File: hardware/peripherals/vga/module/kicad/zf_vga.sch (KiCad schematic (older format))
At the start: 51 parts, among them J2 Z-FIGHTER Expansion Port, J3 DB15_Female, J4 DB9_Male, J5 DB9_Male, SW1 SW_DIP_x03, U1 4040, U10 74HC165, U11 AS6C6264, U12 74HC541, U13 74HC541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

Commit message: VGA Rev. 2
Fixed VGA connector footprint, expanded joystick connectors for '241 buffer, added jumper-selectable interrupt generator
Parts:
- added JP1: Jumper, symbol Device:Jumper
- added Q1: BC547, Package_TO_SOT_THT:TO-92_HandSolder, symbol Transistor_BJT:BC547
- added R10: 1K, Resistor_THT:R_Axial_DIN0207_L6.3mm_D2.5mm_P7.62mm_Horizontal, symbol Device:R
- R1, R2: value R -> 220
- R3: value R -> 200
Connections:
- net DATARDY: now also J2.20 (Pin_20); no longer J2.18 (Pin_18)
- net GND: now also J4.6, J5.6, Q1.3 (E); no longer J4.8, J5.8
- net PA0: now also J4.2, J5.2; no longer J4.1, J5.1
- net PA1: now also J4.3, J5.3; no longer J4.2, J5.2
- net PA2: now also J4.4, J5.4; no longer J4.3, J5.3
- net PA3: now also J4.5, J5.5; no longer J4.4, J5.4
- net PA4: no longer J4.5, J5.5
- net PA5: no longer J4.6, J5.6
- net PC5: now also J4.8; no longer J4.9
- net PC6: now also J5.7; no longer J5.9
- net VCC: now also J4.1, J5.1; no longer J4.7, J5.7
- net PC7: now reaches J2.12 (Pin_12)
- net PC7: now also J5.8
- net #INT: now reaches J2.29 (Pin_29)
- net #INT: now also JP1.2
- net VSYNC: now reaches U4.12 (IO8)
- net VSYNC: now also R10.1
- new net: JP1.1, Q1.1 (C)
- new net: Q1.2 (B), R10.2
- new net PC4: J2.18 (Pin_18), J4.7
- no-connect marks 32 -> 30
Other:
- note added: "Interrupt generator"
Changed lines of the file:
@@
 Text GLabel 7550 3450 2    50   Input ~ 0
 D0
-Text GLabel 7000 5550 0    50   Input ~ 0
-PA0
-Text GLabel 7000 5650 0    50   Input ~ 0
-PA5
 $Comp
 L power:VCC #PWR0116
 U 1 1 622CFD96
-P 6650 5850
-F 0 "#PWR0116" H 6650 5700 50  0001 C CNN
-F 1 "VCC" H 6665 6023 50  0000 C CNN
-F 2 "" H 6650 5850 50  0001 C CNN
-F 3 "" H 6650 5850 50  0001 C CNN
-	1    6650 5850
-	1    0    0    -1
-$EndComp
-Wire Wire Line
-	7000 5850 6650 5850
+P 6650 5550
+F 0 "#PWR0116" H 6650 5400 50  0001 C CNN
+F 1 "VCC" H 6665 5723 50  0000 C CNN
+F 2 "" H 6650 5550 50  0001 C CNN
+F 3 "" H 6650 5550 50  0001 C CNN
+	1    6650 5550
+	1    0    0    -1
+$EndComp
+Wire Wire Line
+	7000 5550 6650 5550
 $Comp
 L power:GND #PWR0135
 U 1 1 622D919E
-P 6650 6050
-F 0 "#PWR0135" H 6650 5800 50  0001 C CNN
-F 1 "GND" H 6655 5877 50  0000 C CNN
-F 2 "" H 6650 6050 50  0001 C CNN
-F 3 "" H 6650 6050 50  0001 C CNN
-	1    6650 6050
-	1    0    0    -1
-$EndComp
-Text GLabel 7000 5750 0    50   Input ~ 0
-PA1
-Text GLabel 7000 5950 0    50   Input ~ 0
-PA2
-Text GLabel 7000 6150 0    50   Input ~ 0
-PA3
-Text GLabel 7000 6350 0    50   Input ~ 0
-PA4
-Text GLabel 7000 6250 0    50   Input ~ 0
-PC5
+P 6650 5650
+F 0 "#PWR0135" H 6650 5400 50  0001 C CNN
+F 1 "GND" H 6655 5477 50  0000 C CNN
+F 2 "" H 6650 5650 50  0001 C CNN
+F 3 "" H 6650 5650 50  0001 C CNN
+	1    6650 5650
+	1    0    0    -1
+$EndComp
 $Comp
 L Connector:DB9_Female J4
@@
 P 5750 4100
 F 0 "R1" H 5820 4146 50  0000 L CNN
-F 1 "R" H 5820 4055 50  0000 L CNN
+F 1 "220" H 5820 4055 50  0000 L CNN
 F 2 "Resistor_THT:R_Axial_DIN0207_L6.3mm_D2.5mm_P7.62mm_Horizontal" V 5680 4100 50  0001 C CNN
 F 3 "~" H 5750 4100 50  0001 C CNN
@@
 P 5750 4450
 F 0 "R2" H 5820 4496 50  0000 L CNN
-F 1 "R" H 5820 4405 50  0000 L CNN
+F 1 "220" H 5820 4405 50  0000 L CNN
 F 2 "Resistor_THT:R_Axial_DIN0207_L6.3mm_D2.5mm_P7.62mm_Horizontal" V 5680 4450 50  0001 C CNN
 F 3 "~" H 5750 4450 50  0001 C CNN
@@
 P 5750 4800
 F 0 "R3" H 5820 4846 50  0000 L CNN
-F 1 "R" H 5820 4755 50  0000 L CNN
+F 1 "200" H 5820 4755 50  0000 L CNN
 F 2 "Resistor_THT:R_Axial_DIN0207_L6.3mm_D2.5mm_P7.62mm_Horizontal" V 5680 4800 50  0001 C CNN
 F 3 "~" H 5750 4800 50  0001 C CNN
@@
 	1    0    0    -1
 $EndComp
-Text Notes 8200 6500 0    50   ~ 0
+Text Notes 8200 6550 0    50   ~ 0
 Controller Port 2
-Text Notes 6450 6500 0    50   ~ 0
+Text Notes 6450 6550 0    50   ~ 0
 Controller Port 1
 Text Notes 8850 4950 0    50   ~ 0
@@
 Text Notes 10500 4950 0    50   ~ 0
 Upper Write Address Buffer
-Text GLabel 8750 6250 0    50   Input ~ 0
-PC6
-Text GLabel 8750 6350 0    50   Input ~ 0
-PA4
-Text GLabel 8750 6150 0    50   Input ~ 0
-PA3
-Text GLabel 8750 5950 0    50   Input ~ 0
-PA2
-Text GLabel 8750 5750 0    50   Input ~ 0
-PA1
-Text GLabel 8750 5650 0    50   Input ~ 0
-PA5
-Text GLabel 8750 5550 0    50   Input ~ 0
-PA0
 $Comp
 L power:GND #PWR0139
 U 1 1 622E4CA3
-P 8400 6050
-F 0 "#PWR0139" H 8400 5800 50  0001 C CNN
-F 1 "GND" H 8405 5877 50  0000 C CNN
-F 2 "" H 8400 6050 50  0001 C CNN
-F 3 "" H 8400 6050 50  0001 C CNN
-	1    8400 6050
-	1    0    0    -1
-$EndComp
-Wire Wire Line
-	8750 6050 8400 6050
-Wire Wire Line
-	8750 5850 8400 5850
+P 8400 5650
+F 0 "#PWR0139" H 8400 5400 50  0001 C CNN
+F 1 "GND" H 8405 5477 50  0000 C CNN
+F 2 "" H 8400 5650 50  0001 C CNN
+F 3 "" H 8400 5650 50  0001 C CNN
+	1    8400 5650
+	1    0    0    -1
+$EndComp
+Wire Wire Line
+	8750 5650 8400 5650
+Wire Wire Line
+	8750 5550 8400 5550
 $Comp
 L power:VCC #PWR0136
 U 1 1 622E4C9B
-P 8400 5850
-F 0 "#PWR0136" H 8400 5700 50  0001 C CNN
-F 1 "VCC" H 8415 6023 50  0000 C CNN
-F 2 "" H 8400 5850 50  0001 C CNN
-F 3 "" H 8400 5850 50  0001 C CNN
-	1    8400 5850
-	1    0    0    -1
-$EndComp
-Text GLabel 10200 2100 0    50   Input ~ 0
-PC6
+P 8400 5550
+F 0 "#PWR0136" H 8400 5400 50  0001 C CNN
+F 1 "VCC" H 8415 5723 50  0000 C CNN
+F 2 "" H 8400 5550 50  0001 C CNN
+F 3 "" H 8400 5550 50  0001 C CNN
+	1    8400 5550
+	1    0    0    -1
+$EndComp
 Text GLabel 10200 2000 0    50   Input ~ 0
 PC5
+Text GLabel 10200 1900 0    50   Input ~ 0
+PC4
 Text GLabel 10200 1500 0    50   Input ~ 0
 PC0
@@
 	1    0    0    -1
 $EndComp
-Text GLabel 10200 1900 0    50   Input ~ 0
+Text GLabel 10200 1800 0    50   Input ~ 0
 DATARDY
 Text GLabel 10950 3950 2    50   Input ~ 0
@@
 NoConn ~ 10150 5950
 Wire Wire Line
-	7000 6050 6650 6050
+	7000 5650 6650 5650
 Wire Wire Line
 	7300 3200 7300 3250
@@
 NoConn ~ 10200 1200
 NoConn ~ 10200 1300
-NoConn ~ 10700 1300
 NoConn ~ 10700 1200
 NoConn ~ 10700 1100
-NoConn ~ 10200 2200
-NoConn ~ 10200 1800
 $Comp
 L Logic_Programmable:GAL16V8 U3
@@
 Text GLabel 3600 3700 2    50   Input ~ 0
 #RESET
-NoConn ~ 3600 4100
 $Comp
 L Memory_RAM:AS6C6264 U11
@@
 Wire Wire Line
 	9650 4350 9950 4350
+Text GLabel 10200 2200 0    50   Input ~ 0
+PC7
+Text GLabel 10200 2100 0    50   Input ~ 0
+PC6
+Text GLabel 8750 6350 0    50   Input ~ 0
+PA3
+Text GLabel 8750 6150 0    50   Input ~ 0
+PA2
+Text GLabel 8750 5950 0    50   Input ~ 0
+PA1
+Text GLabel 8750 5750 0    50   Input ~ 0
+PA0
+Text GLabel 8750 6050 0    50   Input ~ 0
+PC7
+Text GLabel 8750 5850 0    50   Input ~ 0
+PC6
+Text GLabel 7000 6150 0    50   Input ~ 0
+PA2
+Text GLabel 7000 5950 0    50   Input ~ 0
+PA1
+Text GLabel 7000 5750 0    50   Input ~ 0
+PA0
+Text GLabel 7000 6350 0    50   Input ~ 0
+PA3
+Text GLabel 7000 6050 0    50   Input ~ 0
+PC5
+Text GLabel 7000 5850 0    50   Input ~ 0
+PC4
+NoConn ~ 7000 6250
+NoConn ~ 8750 6250
+Text GLabel 3600 4100 2    50   Input ~ 0
+VSYNC
+Text GLabel 13250 5750 2    50   Input ~ 0
+#INT
+Text GLabel 10700 1300 2    50   Input ~ 0
+#INT
+$Comp
+L power:GND #PWR0148
+U 1 1 6253F3E7
+P 12650 6150
+F 0 "#PWR0148" H 12650 5900 50  0001 C CNN
+F 1 "GND" H 12655 5977 50  0000 C CNN
+F 2 "" H 12650 6150 50  0001 C CNN
+F 3 "" H 12650 6150 50  0001 C CNN
+	1    12650 6150
+	1    0    0    -1
+$EndComp
+Text GLabel 12050 5950 0    50   Input ~ 0
+VSYNC
+$Comp
+L Transistor_BJT:BC547 Q1
+U 1 1 6253DD93
+P 12550 5950
+F 0 "Q1" H 12741 5996 50  0000 L CNN
+F 1 "BC547" H 12741 5905 50  0000 L CNN
+F 2 "Package_TO_SOT_THT:TO-92_HandSolder" H 12750 5875 50  0001 L CIN
+F 3 "https://www.onsemi.com/pub/Collateral/BC550-D.pdf" H 12550 5950 50  0001 L CNN
+	1    12550 5950
+	1    0    0    -1
+$EndComp
+Text Notes 12750 6150 0    50   ~ 0
+Interrupt generator
+$Comp
+L Device:R R10
+U 1 1 625772C8
+P 12200 5950
+F 0 "R10" V 12407 5950 50  0000 C CNN
+F 1 "1K" V 12316 5950 50  0000 C CNN
+F 2 "Resistor_THT:R_Axial_DIN0207_L6.3mm_D2.5mm_P7.62mm_Horizontal" V 12130 5950 50  0001 C CNN
+F 3 "~" H 12200 5950 50  0001 C CNN
+	1    12200 5950
+	0    -1   -1   0
+$EndComp
+$Comp
+L Device:Jumper JP1
+U 1 1 62896E08
+P 12950 5750
+F 0 "JP1" H 12950 6014 50  0000 C CNN
+F 1 "Jumper" H 12950 5923 50  0000 C CNN
+F 2 "" H 12950 5750 50  0001 C CNN
+F 3 "~" H 12950 5750 50  0001 C CNN
+	1    12950 5750
+	1    0    0    -1
+$EndComp
 $EndSCHEMATC

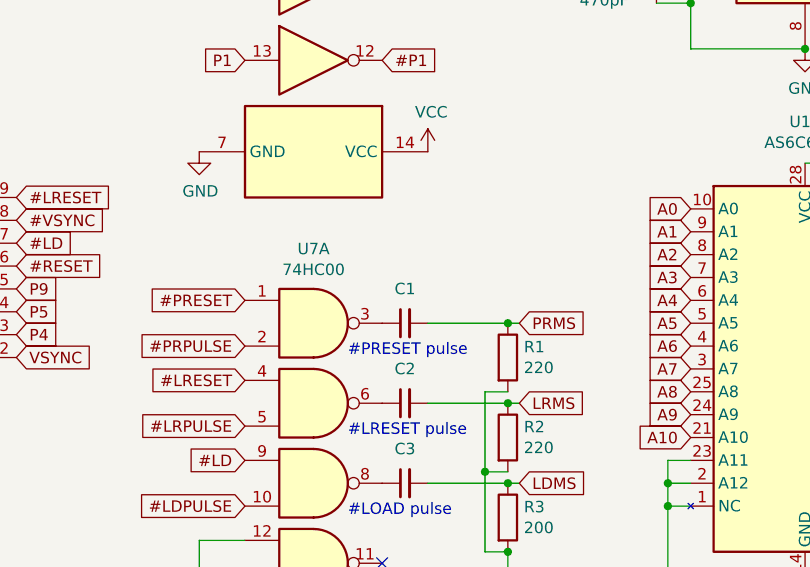
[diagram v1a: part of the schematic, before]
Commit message: Changed Q1 footprint
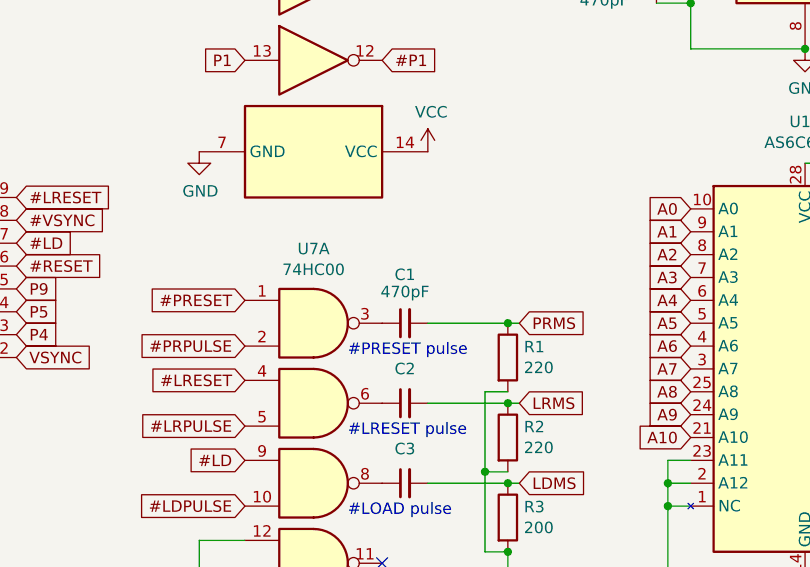
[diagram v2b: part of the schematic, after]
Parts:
- C1, C2, C3: value C_Small -> 470pF
- Q1: footprint Package_TO_SOT_THT:TO-92_HandSolder -> Package_TO_SOT_THT:TO-92_Inline_Wide
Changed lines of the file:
@@
 P 5300 4650
 F 0 "C3" V 5450 4650 50  0000 C CNN
-F 1 "C_Small" V 5437 4650 50  0001 C CNN
+F 1 "470pF" V 5437 4650 50  0001 C CNN
 F 2 "Capacitor_THT:C_Disc_D7.5mm_W2.5mm_P5.00mm" H 5300 4650 50  0001 C CNN
 F 3 "~" H 5300 4650 50  0001 C CNN
@@
 	6450 4750 6450 5050
 $Comp
-L Device:C_Small C1
-U 1 1 6235FCD8
-P 5300 3950
-F 0 "C1" V 5450 3950 50  0000 C CNN
-F 1 "C_Small" V 5437 3950 50  0001 C CNN
-F 2 "Capacitor_THT:C_Disc_D7.5mm_W2.5mm_P5.00mm" H 5300 3950 50  0001 C CNN
-F 3 "~" H 5300 3950 50  0001 C CNN
-	1    5300 3950
-	0    -1   -1   0
-$EndComp
-$Comp
 L Device:C_Small C2
 U 1 1 623621DE
 P 5300 4300
 F 0 "C2" V 5450 4300 50  0000 C CNN
-F 1 "C_Small" V 5437 4300 50  0001 C CNN
+F 1 "470pF" V 5437 4300 50  0001 C CNN
 F 2 "Capacitor_THT:C_Disc_D7.5mm_W2.5mm_P5.00mm" H 5300 4300 50  0001 C CNN
 F 3 "~" H 5300 4300 50  0001 C CNN
@@
 F 0 "Q1" H 12741 5996 50  0000 L CNN
 F 1 "BC547" H 12741 5905 50  0000 L CNN
-F 2 "Package_TO_SOT_THT:TO-92_HandSolder" H 12750 5875 50  0001 L CIN
+F 2 "Package_TO_SOT_THT:TO-92_Inline_Wide" H 12750 5875 50  0001 L CIN
 F 3 "https://www.onsemi.com/pub/Collateral/BC550-D.pdf" H 12550 5950 50  0001 L CNN
 	1    12550 5950
@@
 	1    0    0    -1
 $EndComp
+$Comp
+L Device:C_Small C1
+U 1 1 6235FCD8
+P 5300 3950
+F 0 "C1" V 5512 3950 50  0000 C CNN
+F 1 "470pF" V 5437 3950 50  0000 C CNN
+F 2 "Capacitor_THT:C_Disc_D7.5mm_W2.5mm_P5.00mm" H 5300 3950 50  0001 C CNN
+F 3 "~" H 5300 3950 50  0001 C CNN
+	1    5300 3950
+	0    -1   -1   0
+$EndComp
 $EndSCHEMATC

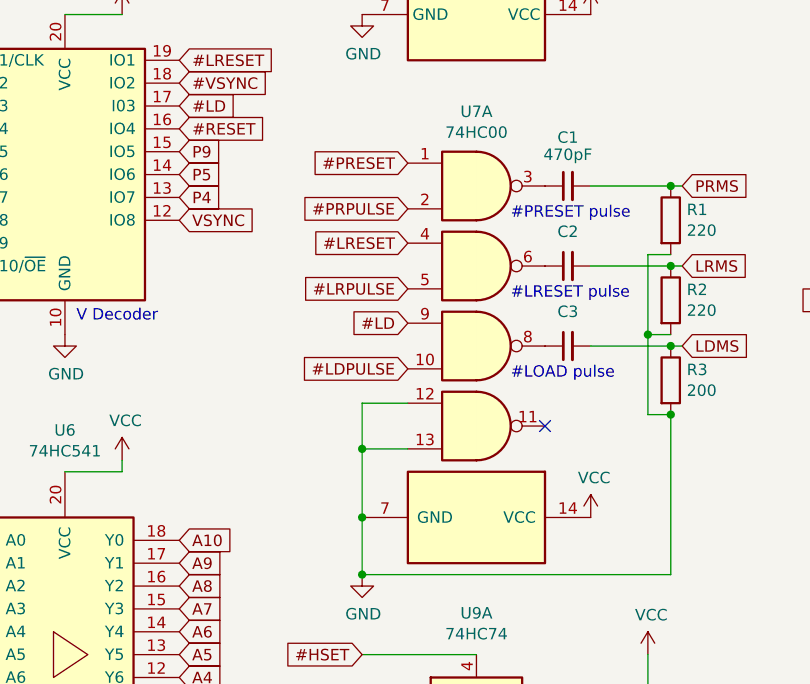
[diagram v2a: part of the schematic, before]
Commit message: Fixed interrupt circuit, routing improvements
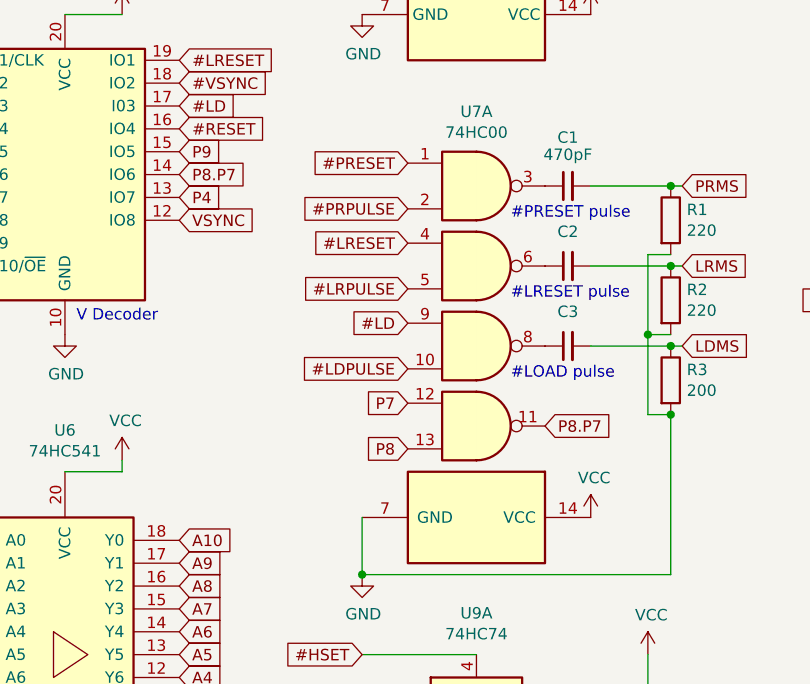
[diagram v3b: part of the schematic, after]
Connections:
- net GND: no longer U7.12, U7.13
- net P5: no longer U4.14 (IO6)
- net P7: now also U7.12
- net P8: now also U7.13
- net P8.P7: now reaches U7.11
- net P8.P7: now also U4.14 (IO6)
- no-connect marks 30 -> 29
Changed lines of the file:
@@
 Text GLabel 950  1450 0    50   Input ~ 0
 PRESET
-Wire Wire Line
-	4600 4900 4400 4900
-Wire Wire Line
-	4400 4900 4400 5100
-Wire Wire Line
-	4600 5100 4400 5100
-Connection ~ 4400 5100
 Text GLabel 4600 2800 0    50   Input ~ 0
 P1
@@
 #HRESET
 Text GLabel 3600 3900 2    50   Input ~ 0
-P5
+P8.P7
 Text GLabel 3600 4000 2    50   Input ~ 0
 P4
@@
 	0    1    1    0
 $EndComp
-Wire Wire Line
-	4400 5100 4400 5400
 Text Notes 5050 4100 0    50   ~ 0
 #PRESET pulse
 Text Notes 5050 4450 0    50   ~ 0
 #LRESET pulse
-Text Notes 5050 4800 0    50   ~ 0
-#LOAD pulse
 $Comp
 L 74xx:74HC00 U7
@@
 	2    4900 4300
 	1    0    0    -1
-$EndComp
-$Comp
-L 74xx:74HC00 U7
-U 5 1 6223A0D4
-P 4900 5400
-F 0 "U7" V 4625 5400 50  0001 C CNN
-F 1 "74HC00" V 4624 5400 50  0001 C CNN
-F 2 "Package_DIP:DIP-14_W7.62mm_LongPads" H 4900 5400 50  0001 C CNN
-F 3 "http://www.ti.com/lit/gpn/sn74hc00" H 4900 5400 50  0001 C CNN
-	5    4900 5400
-	0    1    1    0
 $EndComp
 $Comp
@@
 	0    -1   -1   0
 $EndComp
-NoConn ~ 5200 5000
 Wire Wire Line
 	10700 3450 10450 3450
@@
 Wire Wire Line
 	7300 3200 7300 3250
-Connection ~ 4400 5400
 Wire Wire Line
 	4400 5400 4400 5650
@@
 	0    -1   -1   0
 $EndComp
+Text GLabel 5200 5000 2    50   Input ~ 0
+P8.P7
+Text Notes 5050 4800 0    50   ~ 0
+#LOAD pulse
+Text GLabel 4600 5100 0    50   Input ~ 0
+P8
+Text GLabel 4600 4900 0    50   Input ~ 0
+P7
+$Comp
+L 74xx:74HC00 U7
+U 5 1 6223A0D4
+P 4900 5400
+F 0 "U7" V 4625 5400 50  0001 C CNN
+F 1 "74HC00" V 4624 5400 50  0001 C CNN
+F 2 "Package_DIP:DIP-14_W7.62mm_LongPads" H 4900 5400 50  0001 C CNN
+F 3 "http://www.ti.com/lit/gpn/sn74hc00" H 4900 5400 50  0001 C CNN
+	5    4900 5400
+	0    1    1    0
+$EndComp
 $EndSCHEMATC

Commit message: Schematic media, fixes
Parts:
- R1, R2: value 220 -> 220Ω
- R10: value 1K -> 1KΩ
- R3: value 200 -> 220Ω
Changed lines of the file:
@@
 P 5750 4100
 F 0 "R1" H 5820 4146 50  0000 L CNN
-F 1 "220" H 5820 4055 50  0000 L CNN
+F 1 "220Ω" H 5820 4055 50  0000 L CNN
 F 2 "Resistor_THT:R_Axial_DIN0207_L6.3mm_D2.5mm_P7.62mm_Horizontal" V 5680 4100 50  0001 C CNN
 F 3 "~" H 5750 4100 50  0001 C CNN
@@
 P 5750 4450
 F 0 "R2" H 5820 4496 50  0000 L CNN
-F 1 "220" H 5820 4405 50  0000 L CNN
+F 1 "220Ω" H 5820 4405 50  0000 L CNN
 F 2 "Resistor_THT:R_Axial_DIN0207_L6.3mm_D2.5mm_P7.62mm_Horizontal" V 5680 4450 50  0001 C CNN
 F 3 "~" H 5750 4450 50  0001 C CNN
@@
 P 5750 4800
 F 0 "R3" H 5820 4846 50  0000 L CNN
-F 1 "200" H 5820 4755 50  0000 L CNN
+F 1 "220Ω" H 5820 4755 50  0000 L CNN
 F 2 "Resistor_THT:R_Axial_DIN0207_L6.3mm_D2.5mm_P7.62mm_Horizontal" V 5680 4800 50  0001 C CNN
 F 3 "~" H 5750 4800 50  0001 C CNN
@@
 P 12200 5950
 F 0 "R10" V 12407 5950 50  0000 C CNN
-F 1 "1K" V 12316 5950 50  0000 C CNN
+F 1 "1KΩ" V 12316 5950 50  0000 C CNN
 F 2 "Resistor_THT:R_Axial_DIN0207_L6.3mm_D2.5mm_P7.62mm_Horizontal" V 12130 5950 50  0001 C CNN
 F 3 "~" H 12200 5950 50  0001 C CNN
